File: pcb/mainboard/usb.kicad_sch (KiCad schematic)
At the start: 36 parts, among them J601 USB_A, J602 USB_A, J603 USB_C_Receptacle_USB2.0, J604 USB_B_Micro, U601 USB2514B_Bi, U602 AP2171W, U603 AP2171W, U604 FUSB302BMPX, U605 USBLC6-2P6, Y601 24MHz

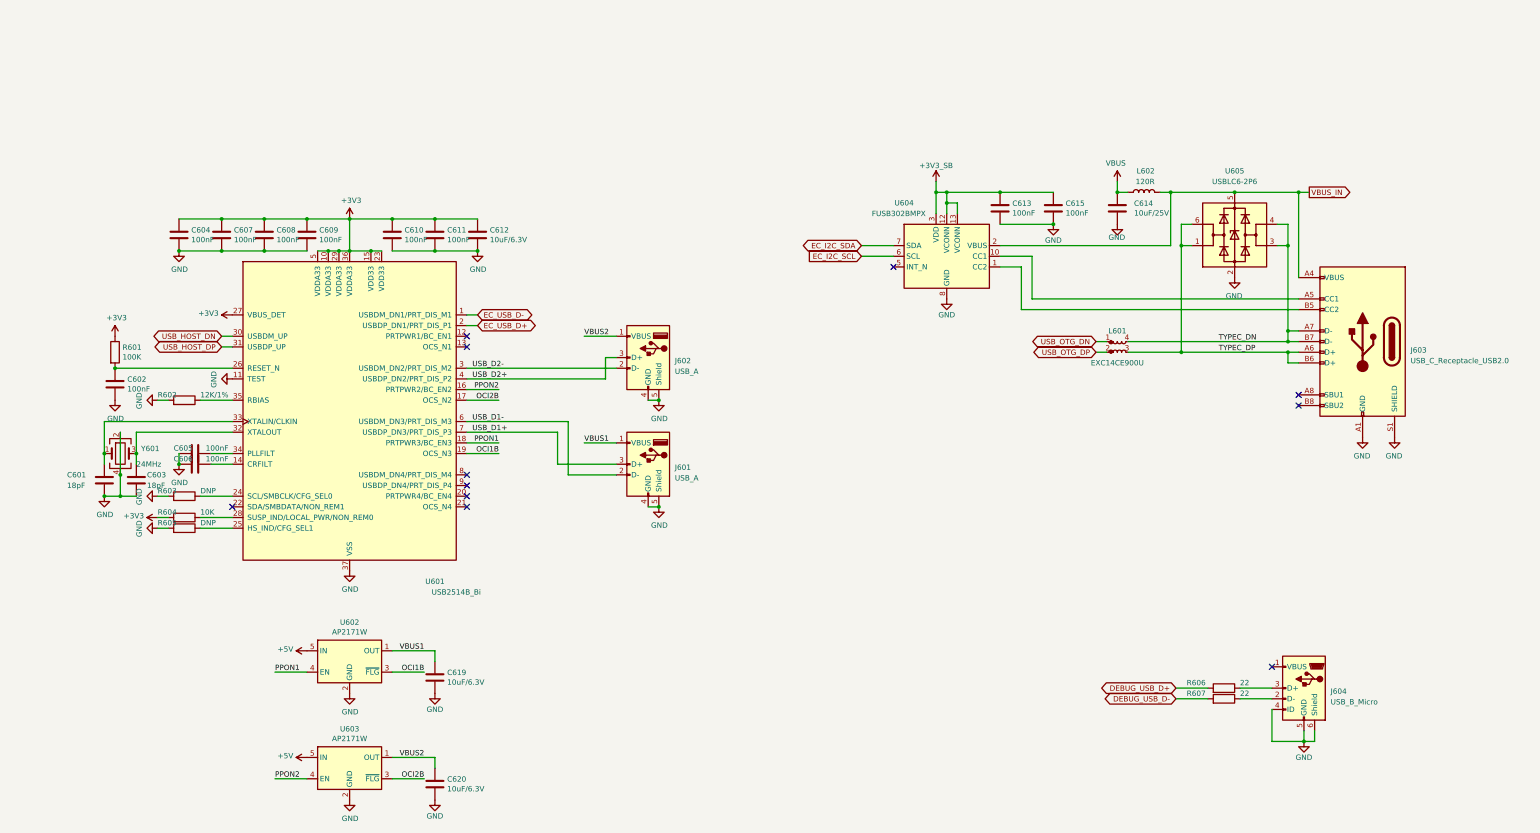
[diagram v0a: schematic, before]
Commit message: pcb: preliminary r0p1 schematics
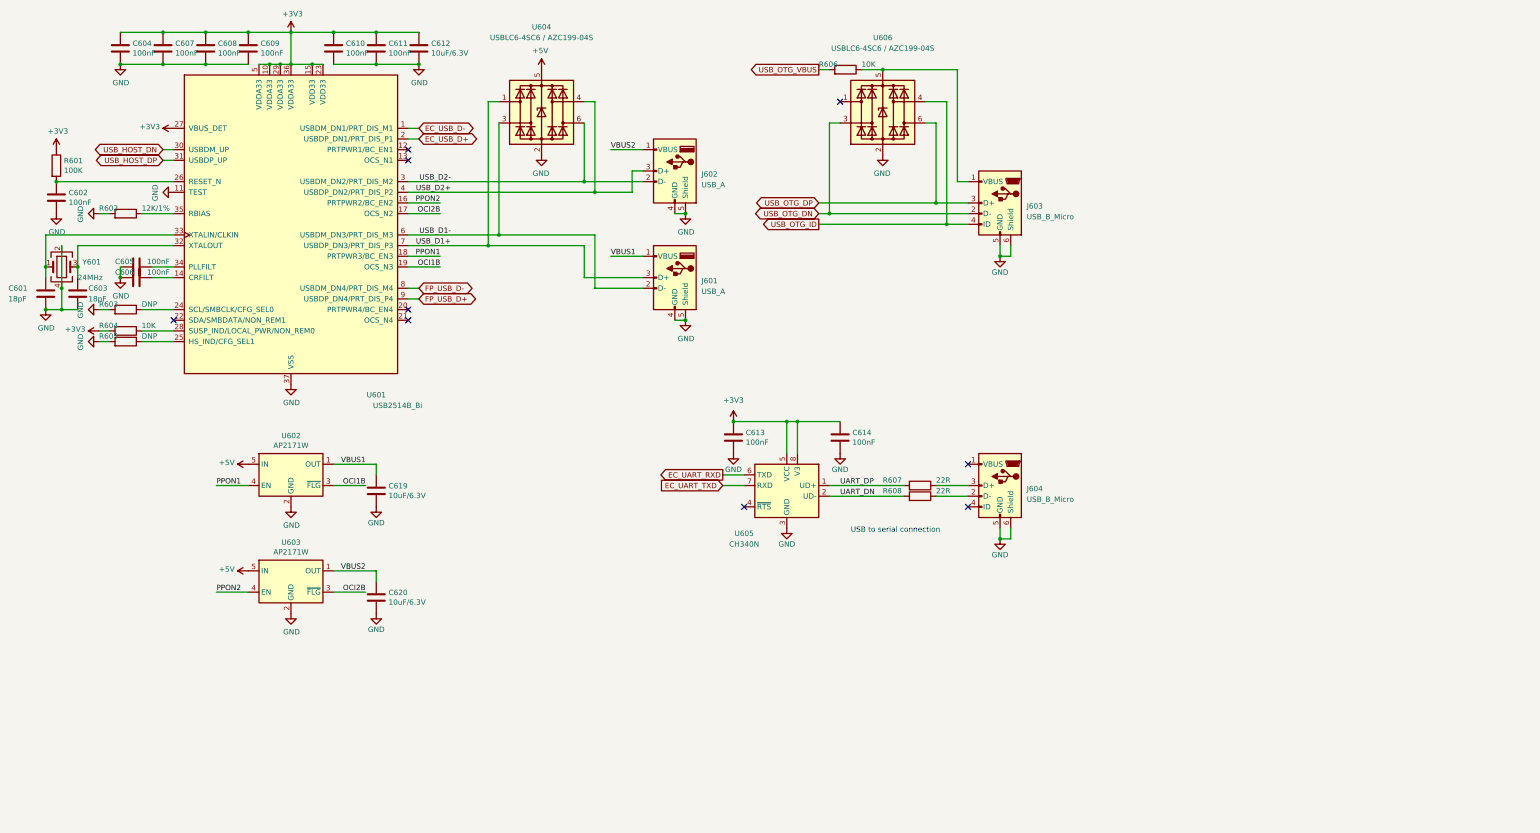
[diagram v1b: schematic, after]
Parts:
- removed C615: 100nF, Capacitor_SMD:C_0402_1005Metric, symbol Device:C
- removed J603: USB_C_Receptacle_USB2.0, Connector_USB:USB_C_Receptacle_HRO_TYPE-C-31-M-12, symbol Connector:USB_C_Receptacle_USB2.0
- removed L601: EXC14CE900U, footprints:L_CommonModeChoke_Panasonic_EXC14CE, symbol Device:L_Coupled_Small_1423
- removed L602: 120R, Inductor_SMD:L_0603_1608Metric, symbol Device:L
- removed U604: FUSB302BMPX, Package_DFN_QFN:WQFN-14-1EP_2.5x2.5mm_P0.5mm_EP1.45x1.45mm, symbol Interface_USB:FUSB302BMPX
- removed U605: USBLC6-2P6, Package_TO_SOT_SMD:SOT-666, symbol Power_Protection:USBLC6-2P6
- added J603: USB_B_Micro, Connector_USB:USB_Micro-B_Amphenol_10103594-0001LF_Horizontal, symbol Connector:USB_B_Micro
- added R608: 22R, Resistor_SMD:R_0402_1005Metric, symbol Device:R
- added U604, U606: USBLC6-4SC6 / AZC199-04S, Package_TO_SOT_SMD:SOT-23-6, symbol Power_Protection:USBLC6-4SC6
- added U605: CH340N, Package_SO:SO-8_3.9x4.9mm_P1.27mm, symbol symbols:CH340N
- C614: value 10uF/25V -> 100nF; footprint Capacitor_SMD:C_0805_2012Metric -> Capacitor_SMD:C_0402_1005Metric
- R606: value 22 -> 10K
- R607: value 22 -> 22R
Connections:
- net +3V3_SB is gone; now on net +3V3: C613.1
- net VBUS is gone; now on net +3V3: C614.1
- net +3V3: now also U605.5 (VCC), U605.8 (V3)
- net +5V: now also U604.5 (VBUS)
- net GND: now also J603.5 (GND), J603.6 (Shield), U604.2 (GND), U605.3 (GND), U606.2 (GND); no longer J604.4 (ID)
- net USB_D1+: now also U604.1 (I/O1)
- net USB_D1-: now also U604.3 (I/O2)
- net USB_D2+: now also U604.4 (I/O3)
- net USB_D2-: now also U604.6 (I/O4)
- net USB_OTG_DN: now also J603.2 (D-), U606.3 (I/O2)
- net USB_OTG_DP: now also J603.3 (D+), U606.6 (I/O4)
- net FP_USB_D-: now reaches U601.8 (USBDM_DN4/PRT_DIS_M4)
- net FP_USB_D+: now reaches U601.9 (USBDP_DN4/PRT_DIS_P4)
- net at R607.1: now also J604.3 (D+); no longer J604.2 (D-)
- net at R606.1: now also J603.1 (VBUS), U606.5 (VBUS); no longer J604.3 (D+)
- net DEBUG_USB_D+ renamed USB_OTG_VBUS
- net DEBUG_USB_D- renamed UART_DP
- net UART_DP: now also U605.1 (UD+)
- new net: J604.2 (D-), R608.1
- new net EC_UART_RXD: U605.6 (TXD)
- new net EC_UART_TXD: U605.7 (RXD)
- new net UART_DN: R608.2, U605.2 (UD-)
- new net USB_OTG_ID: J603.4 (ID), U606.4 (I/O3)
- no-connect marks 11 -> 9
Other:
- note added: "USB to serial connection"
- company: Copyright EI-2030 2021. / Engineer: Wenting Zhang -> Copyright Modos 2021. / Engineer: Wenting Zhang
- moved on the sheet: C601, C602, C603, C604, C605, C606, C607, C608, C609, C610, C611, C612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

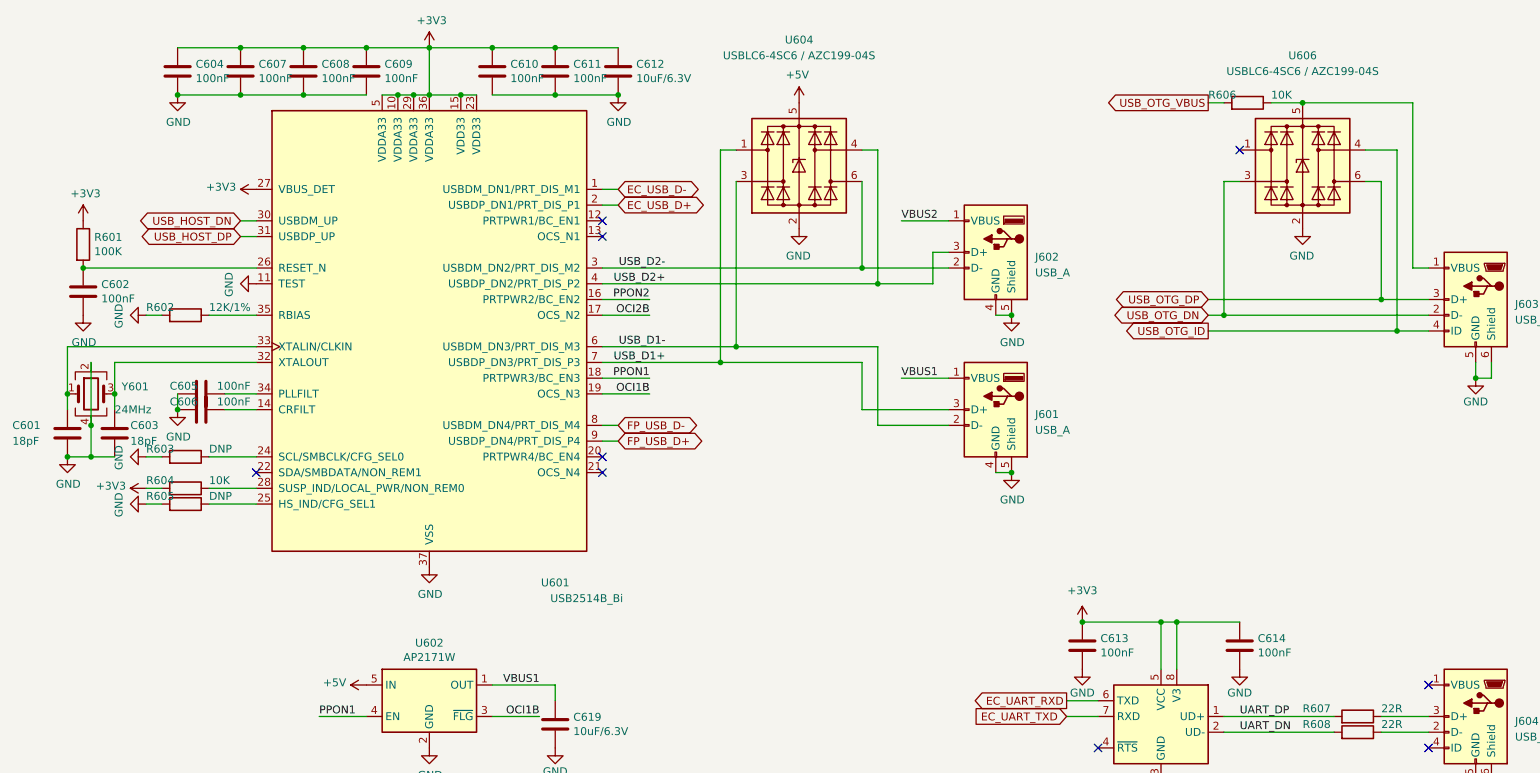
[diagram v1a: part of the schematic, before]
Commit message: pcb: initial placement for mb
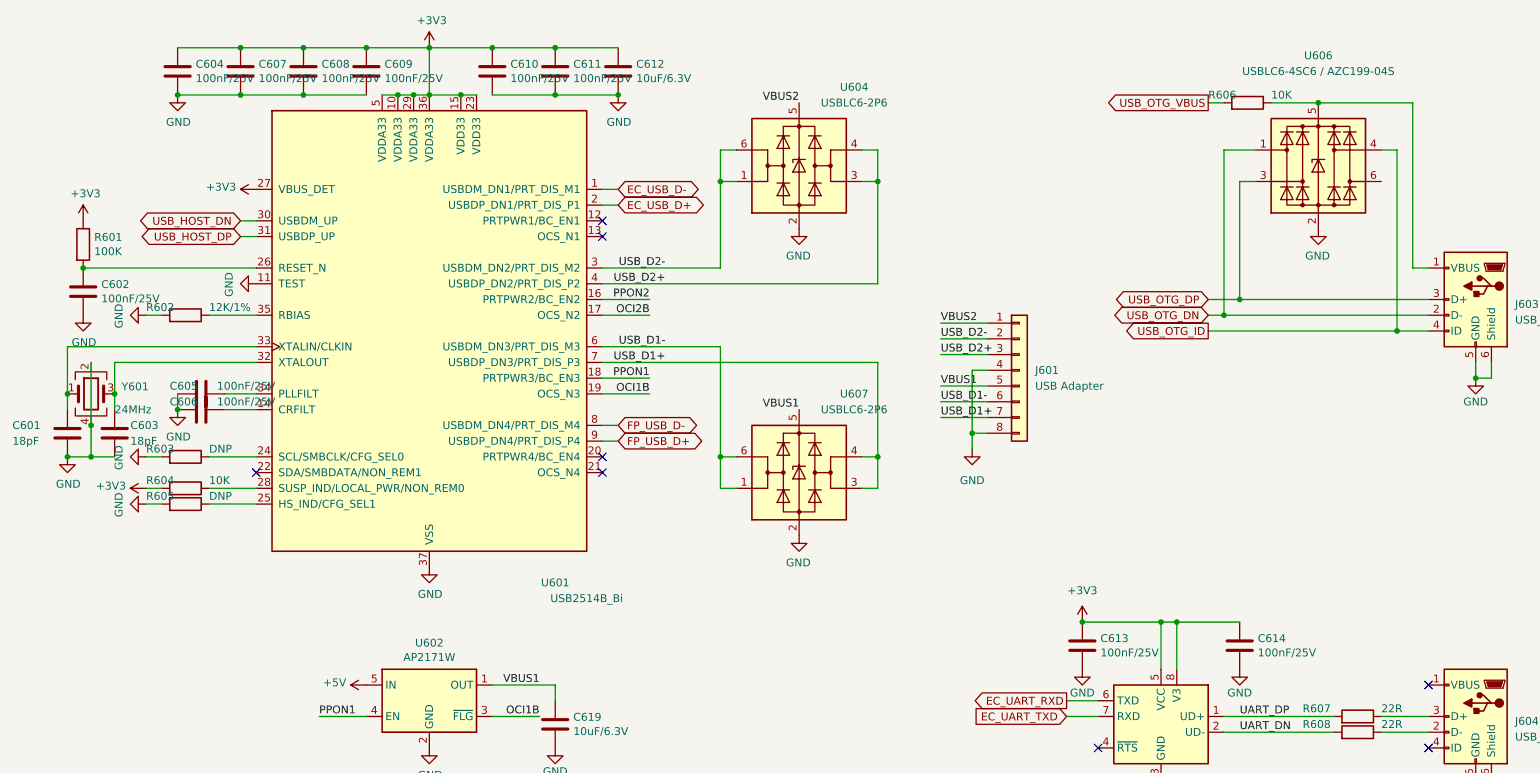
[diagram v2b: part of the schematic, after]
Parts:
- removed J601, J602: USB_A, footprints:Connector_USB_905-562A2021S10100, symbol Connector:USB_A
- removed U604: USBLC6-4SC6 / AZC199-04S, Package_TO_SOT_SMD:SOT-23-6, symbol Power_Protection:USBLC6-4SC6
- added J601: USB Adapter, footprints:USB_Adapter_Board, symbol Connector_Generic:Conn_01x08
- added U604, U607: USBLC6-2P6, Package_TO_SOT_SMD:SOT-666, symbol Power_Protection:USBLC6-2P6
- C601, C603: LCSC (none) -> C182481; Ref.Price (none) -> 0.0061
- C602, C604, C605, C606, C607, C608, C609, C610, C611, C613, C614: value 100nF -> 100nF/25V; LCSC (none) -> C56392; Ref.Price (none) -> 0.0023
- C612, C619, C620: LCSC (none) -> C105490; Ref.Price (none) -> 0.0165
- J603, J604: LCSC (none) -> C428495; Ref.Price (none) -> 0.5627
- R601: LCSC (none) -> C106234; Ref.Price (none) -> 0.0006
- R602: LCSC (none) -> C114760; Ref.Price (none) -> 0.0008
- R603, R605: LCSC (none) -> -; Ref.Price (none) -> 0
- R604, R606: LCSC (none) -> C60489; Ref.Price (none) -> 0.0006
- R607, R608: LCSC (none) -> C93929; Ref.Price (none) -> 0.002
- U601: LCSC (none) -> C220807; Ref.Price (none) -> 2.00
- U602, U603: LCSC (none) -> C110466; Ref.Price (none) -> 0.1114
- U605: LCSC (none) -> C506813; Ref.Price (none) -> 0.4851
- U606: LCSC (none) -> C558419; Ref.Price (none) -> 0.06
- Y601: LCSC (none) -> C555587; Ref.Price (none) -> 0.1982
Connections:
- net GND: now also J601.4 (Pin_4), J601.8 (Pin_8), U604.2 (GND), U607.2 (GND)
- net USB_D1+: now also J601.7 (Pin_7), U607.3 (I/O2), U607.4 (I/O2)
- net USB_D1-: now also J601.6 (Pin_6), U607.1 (I/O1), U607.6 (I/O1)
- net USB_D2+: now also J601.3 (Pin_3), U604.3 (I/O2), U604.4 (I/O2)
- net USB_D2-: now also J601.2 (Pin_2), U604.1 (I/O1), U604.6 (I/O1)
- net USB_OTG_DN: now also U606.1 (I/O1); no longer U606.3 (I/O2)
- net USB_OTG_DP: now also U606.3 (I/O2); no longer U606.6 (I/O4)
- net VBUS1: now also J601.5 (Pin_5), U607.5 (VBUS)
- net VBUS2: now also J601.1 (Pin_1), U604.5 (VBUS)
- no-connect marks 9 -> 8
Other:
- moved on the sheet: U606

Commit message: pcb: r0.1 mb routing done
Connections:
- net GND: now also J601.5 (Pin_5); no longer J601.8 (Pin_8)
- net USB_D1+: now also J601.3 (Pin_3); no longer J601.7 (Pin_7)
- net USB_D1-: now also J601.2 (Pin_2); no longer J601.6 (Pin_6)
- net USB_D2+: now also J601.6 (Pin_6); no longer J601.3 (Pin_3)
- net USB_D2-: now also J601.7 (Pin_7); no longer J601.2 (Pin_2)
- net VBUS1: now also J601.1 (Pin_1); no longer J601.5 (Pin_5)
- net VBUS2: now also J601.8 (Pin_8); no longer J601.1 (Pin_1)
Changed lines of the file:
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@@
   (junction (at 168.91 55.88) (diameter 0) (color 0 0 0 0))
   (junction (at 168.91 100.33) (diameter 0) (color 0 0 0 0))
-  (junction (at 184.15 96.52) (diameter 0) (color 0 0 0 0))
+  (junction (at 184.15 88.9) (diameter 0) (color 0 0 0 0))
   (junction (at 201.93 127) (diameter 0) (color 0 0 0 0))
   (junction (at 214.63 127) (diameter 0) (color 0 0 0 0))
@@
     (stroke (width 0) (type default) (color 0 0 0 0))
   )
-  (wire (pts (xy 184.15 86.36) (xy 184.15 96.52))
-    (stroke (width 0) (type default) (color 0 0 0 0))
-  )
-  (wire (pts (xy 184.15 96.52) (xy 184.15 99.06))
-    (stroke (width 0) (type default) (color 0 0 0 0))
-  )
-  (wire (pts (xy 184.15 96.52) (xy 186.69 96.52))
+  (wire (pts (xy 184.15 86.36) (xy 184.15 88.9))
+    (stroke (width 0) (type default) (color 0 0 0 0))
+  )
+  (wire (pts (xy 184.15 88.9) (xy 184.15 99.06))
+    (stroke (width 0) (type default) (color 0 0 0 0))
+  )
+  (wire (pts (xy 184.15 88.9) (xy 186.69 88.9))
     (stroke (width 0) (type default) (color 0 0 0 0))
   )
@@
     (stroke (width 0) (type default) (color 0 0 0 0))
   )
-  (wire (pts (xy 186.69 88.9) (xy 179.07 88.9))
-    (stroke (width 0) (type solid) (color 0 0 0 0))
-  )
   (wire (pts (xy 186.69 91.44) (xy 179.07 91.44))
     (stroke (width 0) (type solid) (color 0 0 0 0))
@@
     (stroke (width 0) (type solid) (color 0 0 0 0))
   )
+  (wire (pts (xy 186.69 96.52) (xy 179.07 96.52))
+    (stroke (width 0) (type solid) (color 0 0 0 0))
+  )
   (wire (pts (xy 199.39 139.7) (xy 204.47 139.7))
     (stroke (width 0) (type solid) (color 0 0 0 0))
@@
     (effects (font (size 1.27 1.27)) (justify right bottom))
   )
-  (label "VBUS2" (at 179.07 78.74 0)
-    (effects (font (size 1.27 1.27)) (justify left bottom))
-  )
-  (label "USB_D2-" (at 179.07 81.28 0)
-    (effects (font (size 1.27 1.27)) (justify left bottom))
-  )
-  (label "USB_D2+" (at 179.07 83.82 0)
-    (effects (font (size 1.27 1.27)) (justify left bottom))
-  )
-  (label "VBUS1" (at 179.07 88.9 0)
-    (effects (font (size 1.27 1.27)) (justify left bottom))
-  )
-  (label "USB_D1-" (at 179.07 91.44 0)
-    (effects (font (size 1.27 1.27)) (justify left bottom))
-  )
-  (label "USB_D1+" (at 179.07 93.98 0)
-    (effects (font (size 1.27 1.27)) (justify left bottom))
-  )
+  (label "VBUS1" (at 179.07 78.74 0)
+    (effects (font (size 1.27 1.27)) (justify left bottom))
+  )
+  (label "USB_D1-" (at 179.07 81.28 0)
+    (effects (font (size 1.27 1.27)) (justify left bottom))
+  )
+  (label "USB_D1+" (at 179.07 83.82 0)
+    (effects (font (size 1.27 1.27)) (justify left bottom))
+  )
+  (label "USB_D2+" (at 179.07 91.44 0)
+    (effects (font (size 1.27 1.27)) (justify left bottom))
+  )
+  (label "USB_D2-" (at 179.07 93.98 0)
+    (effects (font (size 1.27 1.27)) (justify left bottom))
+  )
+  (label "VBUS2" (at 179.07 96.52 0)
+    (effects (font (size 1.27 1.27)) (justify left bottom))
+  )
